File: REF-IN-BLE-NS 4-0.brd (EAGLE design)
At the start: 44 parts, among them U1 NRF52832_10QFN48, U2 AEM10941, X1 FA-128-32MHZMF10Z-AJ5

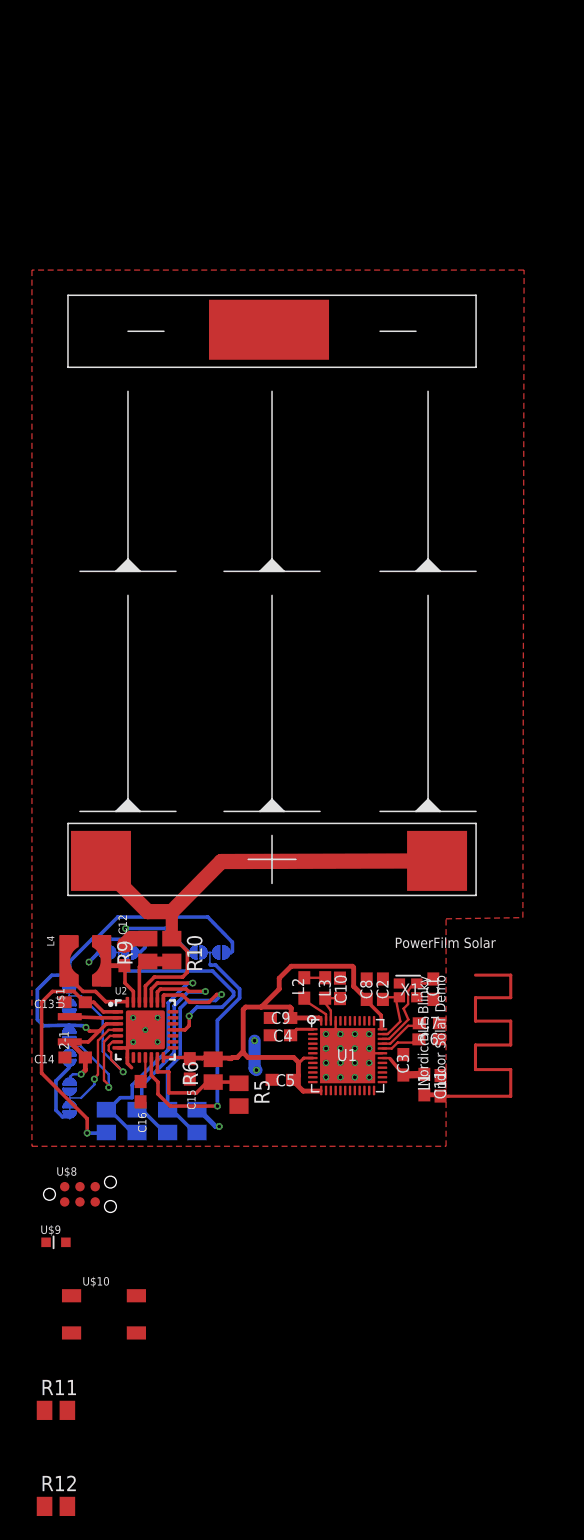
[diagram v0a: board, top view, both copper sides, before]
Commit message: Added caps and prettied up
Documentation is still needed, will add that as an issue
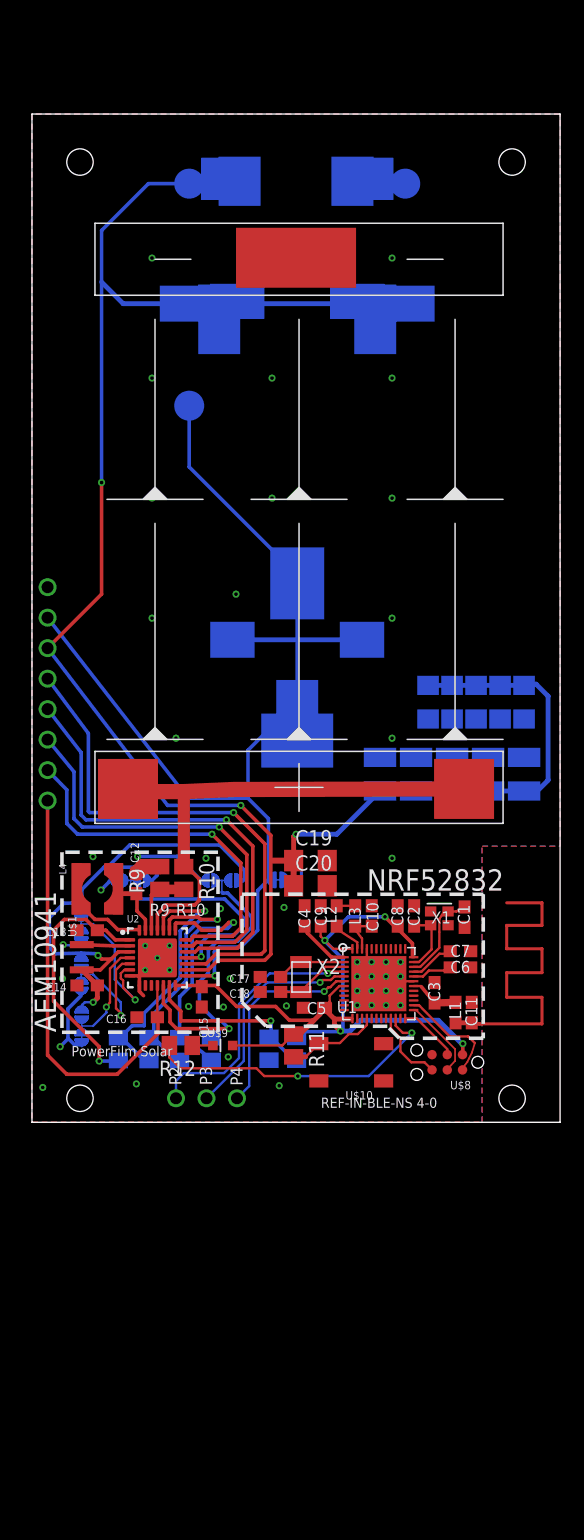
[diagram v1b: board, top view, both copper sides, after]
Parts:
- added C17, C18: 12pF, resistor:C0603
- added C19, C20: 220uF, resistor:C1206
- added C21, C22, C23, C24, C25: (no value), resistor:C1206
- added C26, C27, C28, C29, C30: (no value), resistor:C1210
- added U$11: SOLDER_BRIGDECLOSED, 00_PF_Nordic:SOLDER_BRIDGE_CLOSED
- added U$12, U$13, U$14, U$15, U$16, U$17, U$18, U$19, U$20, U$21, U$22: 1MM_PAD, 00_PF_Nordic:1MM_PAD
- added U$23: CAP-XX_A-TYPE, 00_PF_Nordic:CAP-XX_A-TYPE
- added U$24: CAP-XX_S-TYPE, 00_PF_Nordic:CAP-XX_S-TYPE
- added U$25: CAP-XX_W-TYPE, 00_PF_Nordic:CAP-XX_W-TYPE
- added U$26: BZ01_L-TYPE, 00_PF_Nordic:BZ01_L-TYPE
- added U$27: BZ059_N-TYPE, 00_PF_Nordic:BZ059_N-TYPE
- added U$28: BZ01_S-TYPE, 00_PF_Nordic:BZ01_S-TYPE
- added U$29: BZ05_S-TYPE, 00_PF_Nordic:BZ05_S-TYPE
- added U$30: BZ09_S-TYPE, 00_PF_Nordic:BZ09_S-TYPE
- added X2: 32.768k, 00_PF_Nordic:FC-135
- moved R12 39.8 mm to (12.4, 8.40), turned to 180 degrees
- moved R11 36.3 mm to (21.8, 8.40), turned to 270 degrees
- moved U$8 32.5 mm to (34.6, 7.00), turned to 180 degrees
- moved U$10 29.4 mm to (26.6, 7.00), turned to 180 degrees
- moved U$9 21.5 mm to (15.9, 8.40)
- moved C4 10.1 mm to (22.7, 19.2), turned to 90 degrees
- moved C9 9.14 mm to (24.1, 19.2), turned to 90 degrees
- moved R6 7.19 mm to (22.1, 8.12), flipped to the bottom
- moved C2 6.63 mm to (31.8, 19.2)
- moved C11 6.63 mm to (36.6, 11.1)
- moved C8 6.62 mm to (30.5, 19.2)
- moved C10 6.59 mm to (28.3, 19.2)
- moved L2 6.58 mm to (25.4, 19.2)
- moved AE1 6.56 mm to (37.1, 10.2)
- moved C6 6.54 mm to (35.7, 14.9)
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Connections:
- removed net N$34: U2.15
- new net BAL: U$11.P$1, U$19.P$1, U$23.P$1, U$24.P$1, U$25.P$1, U$26.P$3, U$26.P$4, U$28.P$3, U$29.P$3, U$30.P$3, U2.15
- new net BATT: C19.1, C20.1, C21.1, C22.1, C23.1, C24.1, C25.1, C26.1, C27.1, C28.1, C29.1, C30.1, U$18.P$1, U$23.P$2, U$24.P$2, U$25.P$2, U$26.P$1, U$26.P$2, U$27.P$1, U$28.P$1, U$28.P$2, U$29.P$1, U$29.P$2, U$30.P$1, U$30.P$2, U2.16
- new net N$36: C17.1, U1.2, X2.P$1
- new net N$37: C18.1, U1.3, X2.P$2
- new net N$38: U$20.P$1, U1.4
- new net N$39: U$13.P$1, U2.19
- new net N$40: U$14.P$1, U2.20
- new net N$41: U$15.P$1, U2.21
- new net N$42: U$21.P$1, U1.5
- new net N$43: U$22.P$1, U1.6
- net GND: now also C17.2, C18.2, C19.2, C20.2, C21.2, C22.2, C23.2, C24.2, C25.2, C26.2, C27.2, C28.2, C29.2, C30.2, U$11.P$2, U$17.P$1, U$23.P$3, U$24.P$3, U$25.P$3, U$27.P$2
- net LVOUT: now also U$16.P$1
- net N$33: now also U$12.P$1, U2.17; no longer U2.16
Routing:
- net BATT: track 0.00 -> 172.9 mm, vias 0 -> 3
- net BAL: track 0.00 -> 98.8 mm, vias 0 -> 1
- net N$33: track 0.00 -> 44.0 mm, vias 0 -> 1
- net N$39: track 0.00 -> 38.6 mm, vias 0 -> 1
- net N$40: track 0.00 -> 34.9 mm, vias 0 -> 1
- net LVOUT: track 2.31 -> 36.5 mm
- net N$41: track 0.00 -> 31.5 mm, vias 0 -> 1
- net N$31: track 0.00 -> 25.5 mm, vias 0 -> 2
- net N$38: track 0.00 -> 21.9 mm, vias 0 -> 1
- net N$42: track 0.00 -> 18.4 mm, vias 0 -> 1
- net HVOUT: track 52.2 -> 70.1 mm, vias 0 -> 4
- net N$43: track 0.00 -> 16.8 mm, vias 0 -> 1
- net N$24: track 0.00 -> 8.92 mm
- net N$17: track 0.00 -> 7.95 mm
- net N$21: track 0.00 -> 6.78 mm
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- added copper zone on layer 16, net GND
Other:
- board outline added: 44 x 84 mm
- board text added: "+"
- board text added: "-"
- board text added: "AEM10941"
- board text added: "BAL"
- board text added: "BATT"
- board text added: "CFG0"
- board text added: "CFG1"
- board text added: "CFG2"
- board text added: "ENBAL"
- board text added: "ENHV"
- board text added: "ENLV"
- board text added: "GND"
- board text added: "LVOUT"
- board text added: "NRF52832"
- board text added: "P2"
- board text added: "P3"
- board text added: "P4"
- board text added: "PRIM"
- board text added: "R1"
- board text added: "R10"
- board text added: "R2"
- board text added: "R3"
- board text added: "R4"
- board text added: "R5"
- board text added: "R6"
- board text added: "R9"
- board text added: "REF-IN-BLE-NS 4-0"
- board text added: "STATUS0"
- board text added: "STATUS1"
- board text added: "STATUS2"
- board text removed: "2-1"
- board text removed: "Indoor Solar Demo"
- board text removed: "Nordic BLE Blinky"

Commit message: Fixed grounding and added labels
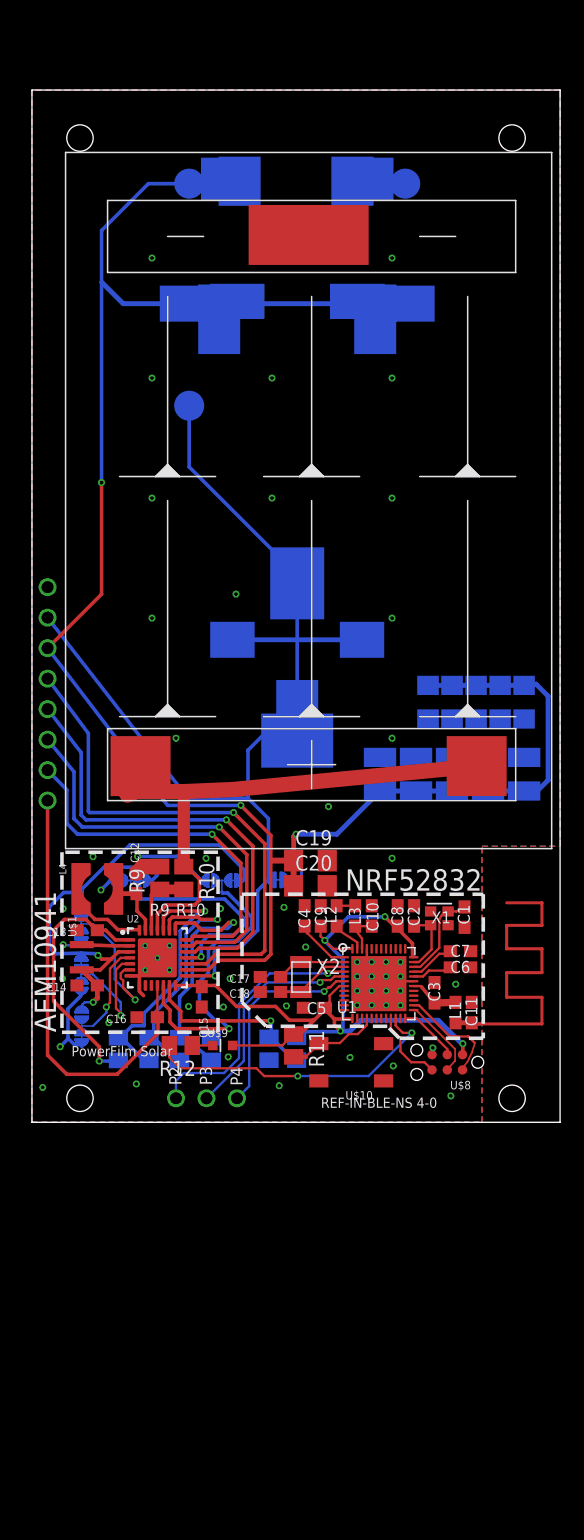
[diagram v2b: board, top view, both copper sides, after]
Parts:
- moved U$7 33.6 mm to (23.1, 53.8)
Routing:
- net N$29: track 46.4 -> 49.3 mm
- net VBUCK: track 43.9 -> 44.9 mm
- net GND: track 34.3 -> 34.5 mm, vias 31 -> 40
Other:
- board size 44 x 84 mm -> 44 x 86 mm
- board text added: "1206"
- board text added: "1210"

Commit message: Modified top cream
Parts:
- L4: value (none) -> 22uH
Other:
- board text added: "Indoor Solar Reference Design w/ Nordic BLE and E-peas Energy Harvester"
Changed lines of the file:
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@@
 <setting verticaltext="up"/>
 </settings>
-<grid distance="0.025" unitdist="mm" unit="mm" style="dots" multiple="1" display="yes" altdistance="0.003125" altunitdist="mic" altunit="mm"/>
+<grid distance="0.05" unitdist="mm" unit="mm" style="dots" multiple="1" display="yes" altdistance="0.003125" altunitdist="mic" altunit="mm"/>
 <layers>
-<layer number="1" name="Top" color="4" fill="1" visible="no" active="yes"/>
+<layer number="1" name="Top" color="4" fill="1" visible="yes" active="yes"/>
 <layer number="2" name="Route2" color="1" fill="3" visible="no" active="no"/>
 <layer number="3" name="Route3" color="4" fill="3" visible="no" active="no"/>
@@
 <layer number="15" name="Route15" color="4" fill="6" visible="no" active="no"/>
 <layer number="16" name="Bottom" color="1" fill="1" visible="yes" active="yes"/>
-<layer number="17" name="Pads" color="2" fill="1" visible="no" active="yes"/>
-<layer number="18" name="Vias" color="2" fill="1" visible="no" active="yes"/>
+<layer number="17" name="Pads" color="2" fill="1" visible="yes" active="yes"/>
+<layer number="18" name="Vias" color="2" fill="1" visible="yes" active="yes"/>
 <layer number="19" name="Unrouted" color="6" fill="1" visible="no" active="yes"/>
-<layer number="20" name="Dimension" color="15" fill="1" visible="no" active="yes"/>
-<layer number="21" name="tPlace" color="7" fill="1" visible="no" active="yes"/>
+<layer number="20" name="Dimension" color="15" fill="1" visible="yes" active="yes"/>
+<layer number="21" name="tPlace" color="7" fill="1" visible="yes" active="yes"/>
 <layer number="22" name="bPlace" color="7" fill="1" visible="yes" active="yes"/>
-<layer number="23" name="tOrigins" color="15" fill="1" visible="no" active="yes"/>
+<layer number="23" name="tOrigins" color="15" fill="1" visible="yes" active="yes"/>
 <layer number="24" name="bOrigins" color="15" fill="1" visible="no" active="yes"/>
 <layer number="25" name="tNames" color="7" fill="1" visible="no" active="yes"/>
@@
 <layer number="27" name="tValues" color="7" fill="1" visible="no" active="yes"/>
 <layer number="28" name="bValues" color="7" fill="1" visible="no" active="yes"/>
-<layer number="29" name="tStop" color="7" fill="3" visible="no" active="yes"/>
+<layer number="29" name="tStop" color="7" fill="3" visible="yes" active="yes"/>
 <layer number="30" name="bStop" color="7" fill="6" visible="no" active="yes"/>
-<layer number="31" name="tCream" color="7" fill="4" visible="no" active="yes"/>
+<layer number="31" name="tCream" color="7" fill="4" visible="yes" active="yes"/>
 <layer number="32" name="bCream" color="7" fill="5" visible="no" active="yes"/>
 <layer number="33" name="tFinish" color="6" fill="3" visible="no" active="yes"/>
@@
 <board>
 <plain>
-<text x="33.76" y="4.055" size="0.85" layer="21" font="vector" ratio="10" rot="R180">REF-IN-BLE-NS 4-0</text>
-<text x="11.715" y="8.35" size="0.85" layer="21" font="vector" ratio="10" rot="R180">PowerFilm Solar</text>
+<text x="1.9" y="51.265" size="0.85" layer="21" font="vector" ratio="10" rot="R90">REF-IN-BLE-NS 4-0</text>
+<text x="1.9" y="65.735" size="0.85" layer="21" font="vector" ratio="10" rot="R90">PowerFilm Solar</text>
 <text x="25.4" y="11.1" size="1" layer="25" font="vector">U1</text>
 <wire x1="2.5" y1="24.5" x2="2.5" y2="9.5" width="0.3" layer="21" style="shortdash"/>
@@
 <rectangle x1="41.76015" y1="11.66655" x2="41.87445" y2="11.67925" layer="22"/>
 <rectangle x1="41.78555" y1="11.65385" x2="41.83635" y2="11.66655" layer="22"/>
+<text x="6.5" y="84.5" size="0.85" layer="21" font="vector">Indoor Solar Reference Design
+w/ Nordic BLE and E-peas Energy Harvester</text>
 </plain>
 <attributes>
@@
 <attribute name="VALUE" x="28.835" y="18.555" size="1.27" layer="27" rot="R90"/>
 </element>
-<element name="U1" library="00_PF_Nordic" package="NRF52832_10" value="NRF52832_10QFN48" x="28.9" y="13.55" smashed="yes"/>
+<element name="U1" library="00_PF_Nordic" package="NRF52832_10" value="NRF52832_10QFN48" x="28.9" y="13.55" smashed="yes">
+<attribute name="MFG_PART#" value="NRF52832-QFAA-R" x="28.9" y="13.55" size="1.778" layer="27" display="off"/>
+</element>
 <element name="X1" library="00_PF_Nordic" package="FA-128-EPSON" value="FA-128-32MHZMF10Z-AJ5" x="33.94" y="18.99" smashed="yes">
 <attribute name="NAME" x="33.265" y="18.565" size="1" layer="25" font="vector"/>
@@
 <attribute name="MFG_PART#" value="" x="36.64" y="11.14" size="1.778" layer="27" rot="R90" display="off"/>
 </element>
-<element name="U2" library="00_PF_Nordic" package="QFN28_5X5_05PITCH" value="AEM10941" x="10.45" y="15.7"/>
+<element name="U2" library="00_PF_Nordic" package="QFN28_5X5_05PITCH" value="AEM10941" x="10.45" y="15.7">
+<attribute name="MFG_PART#" value="AEM10941-QFN " x="10.45" y="15.7" size="1.778" layer="27" display="off"/>
+</element>
 <element name="C12" library="resistor" package="C0603" value="10uF" x="8.7" y="21.9" rot="R90">
 <attribute name="PERCENTAGE" value="" x="8.7" y="21.9" size="1.778" layer="27" rot="R90" display="off"/>
@@
 <element name="R10" library="resistor" package="M0805" value="0" x="12.65" y="22.35" rot="R270"/>
 <element name="U$7" library="00_PF_Nordic" package="SOLAR_CELL_37X54MM" value="SOLAR_CELL" x="23.05" y="53.8" rot="R90"/>
-<element name="L4" library="00_PF_Nordic" package="744031220" value="" x="5.45" y="21.45" rot="R270">
+<element name="L4" library="00_PF_Nordic" package="744031220" value="22uH" x="5.45" y="21.45" rot="R270">
 <attribute name="PERCENTAGE" value="30%" x="5.45" y="21.45" size="1.778" layer="27" rot="R270" display="off"/>
 <attribute name="MFG_PART#" value="744031220" x="5.45" y="21.45" size="1.778" layer="27" rot="R270" display="off"/>
@@
 </board>
 </drawing>
+<compatibility>
+<note version="6.3" minversion="6.2.2" severity="warning">
+Since Version 6.2.2 text objects can contain more than one line,
+which will not be processed correctly with this version.
+</note>
+</compatibility>
 </eagle>

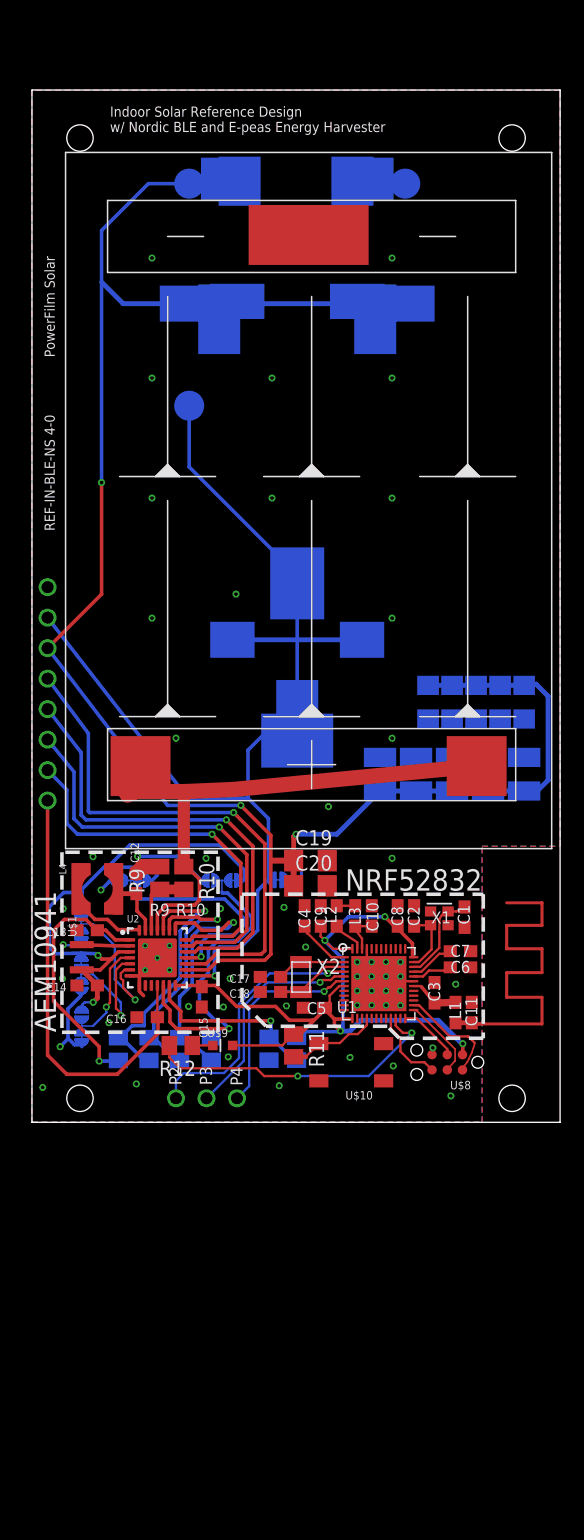
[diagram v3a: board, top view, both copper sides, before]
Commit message: Added MPNs to Device Technologies
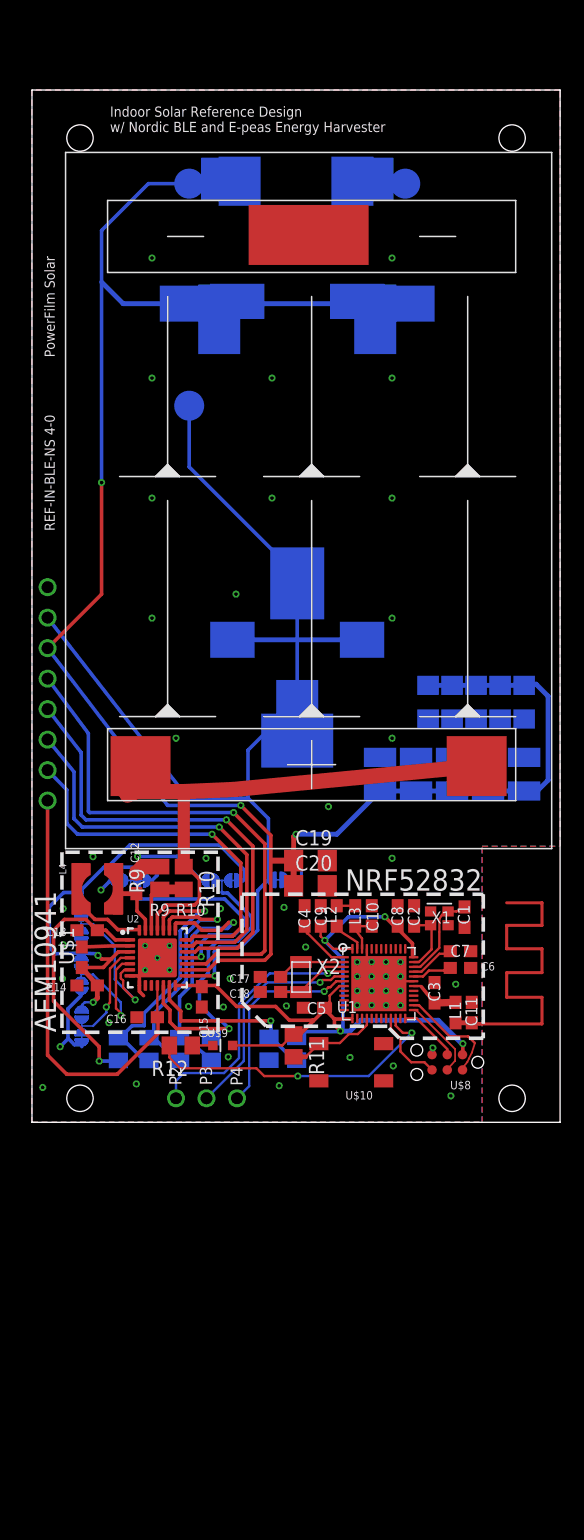
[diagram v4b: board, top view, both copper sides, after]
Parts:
- R10, R11, R12: device resistor:M0805 -> resistor:R0805
- U$1: value 10uF -> 10uH; device 00_PF_Nordic:L1007 -> 00_PF_Nordic:L0603
- U$10: value MJTP1140 -> (none)
- U$9: value APT1608LZGCK -> N/A
- X1: value FA-128-32MHZMF10Z-AJ5 -> 32 MHz
- X2: value 32.768k -> 32.768 kHz
- moved C6 0.05 mm to (35.7, 14.9)
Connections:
- net N$15: now also U$1.2; no longer U$1.P$2
- net VBUCK: now also U$1.1; no longer U$1.P$1
